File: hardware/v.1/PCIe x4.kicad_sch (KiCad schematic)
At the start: 18 parts, among them J2 Bus_PCI_Express_x4

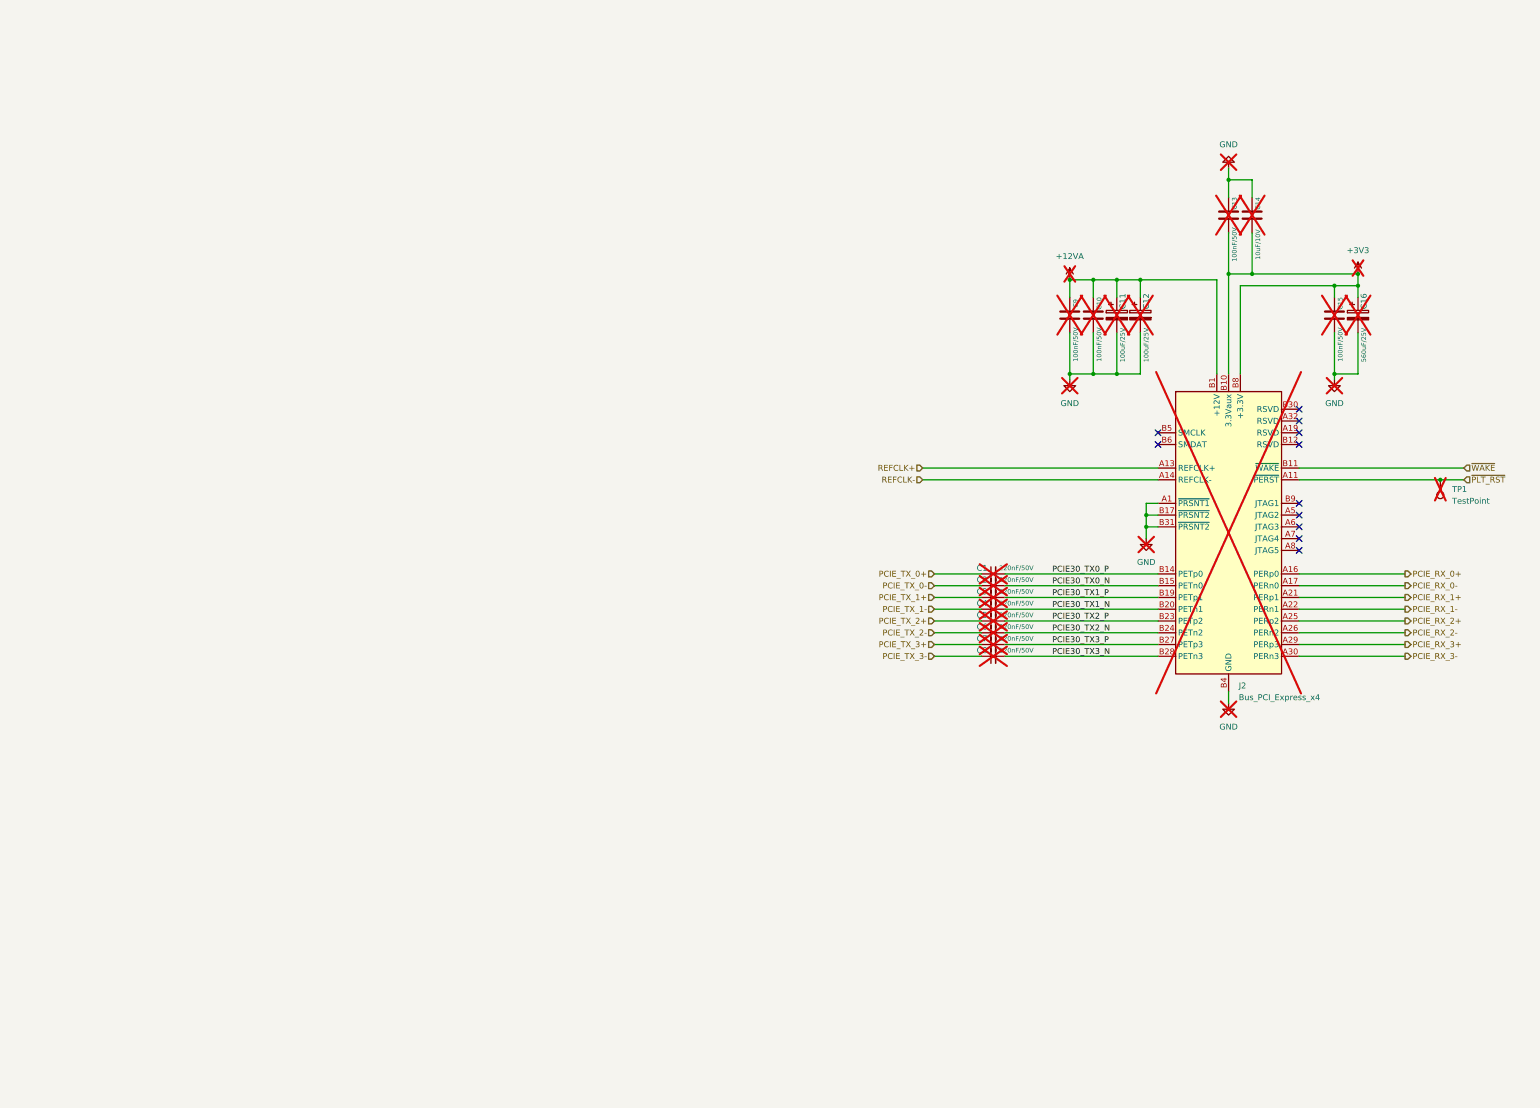
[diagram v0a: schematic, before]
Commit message: pretty much finish the board, did bios chip, gpio, 4x sata
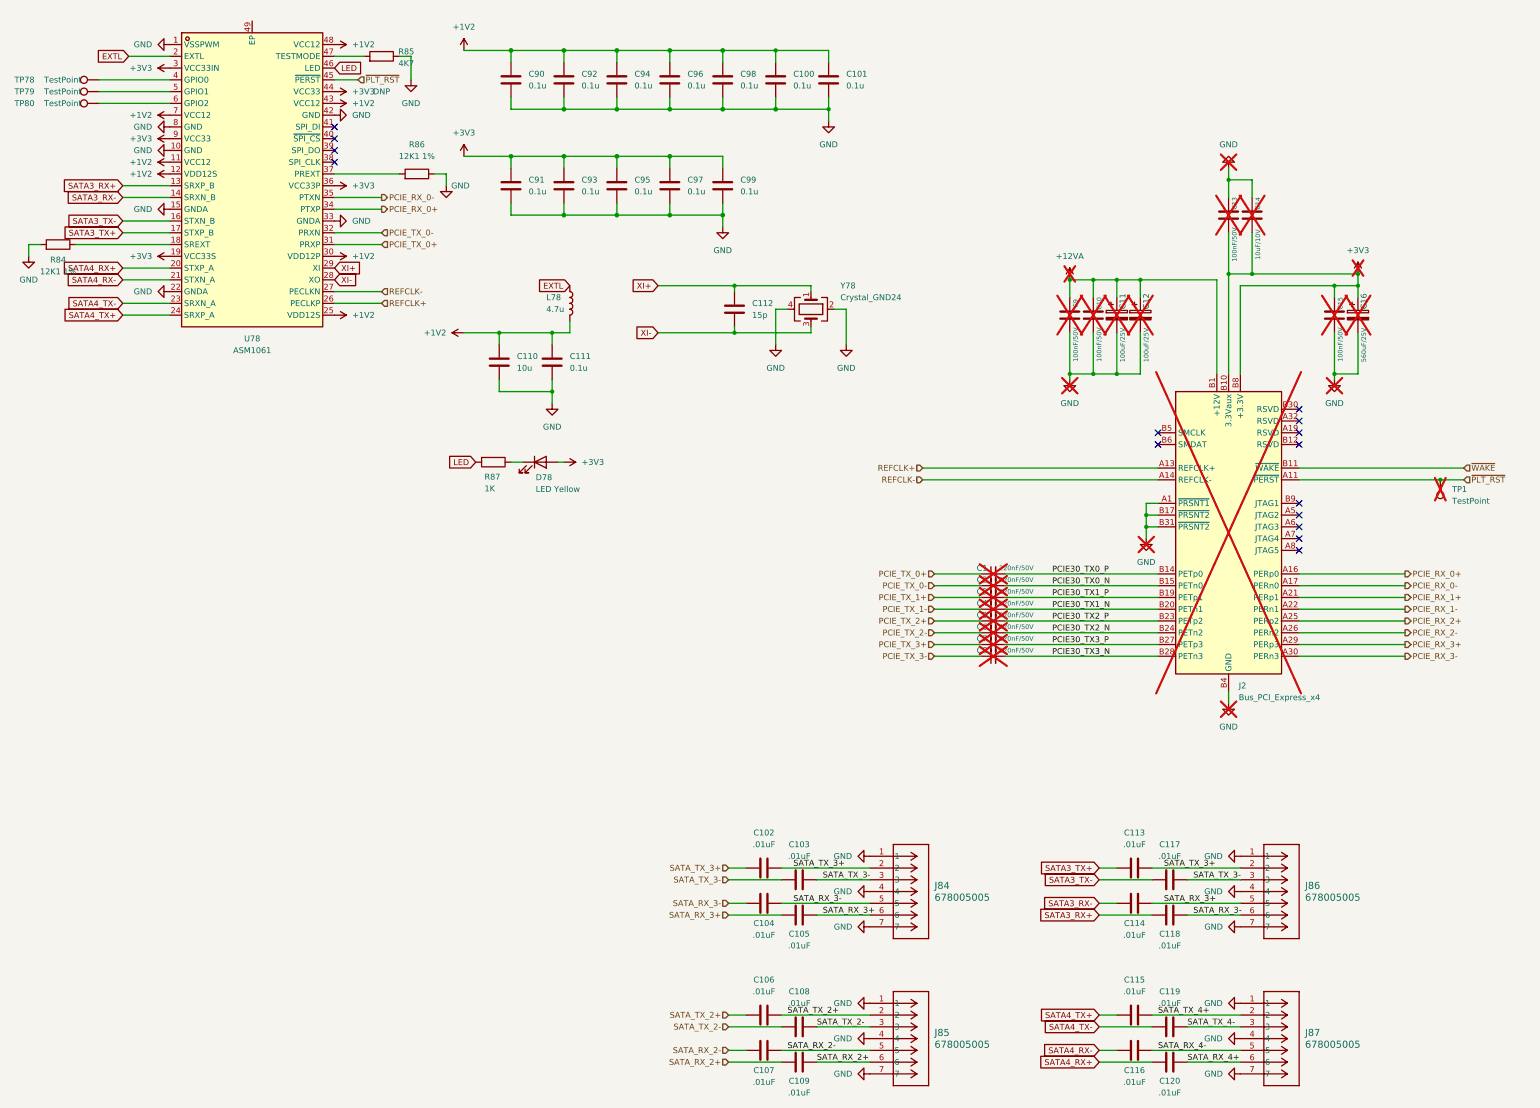
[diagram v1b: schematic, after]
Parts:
- added C100, C101, C111, C90, C91, C92, C93, C94, C95, C96, C97, C98, C99: 0.1u, Capacitor_SMD:C_0402_1005Metric, symbol Device:C
- added C102, C103, C104, C105, C106, C107, C108, C109, C113, C114, C115, C116, C117, C118, C119, C120: .01uF, Capacitor_SMD:C_0402_1005Metric, symbol Device:C
- added C110: 10u, Capacitor_SMD:C_0805_2012Metric, symbol Device:C
- added C112: 15p, Capacitor_SMD:C_0402_1005Metric, symbol Device:C
- added D78: LED Yellow, LED_SMD:LED_0603_1608Metric, symbol Device:LED
- added J84, J85, J86, J87: 678005005, SATA 7PIN:CONN_67800-5005_MOL, symbol 2025-07-27_04-45-58:678005005
- added L78: 4.7u, Inductor_SMD:L_1008_2520Metric, symbol Device:L
- added R84, R86: 12K1 1%, Resistor_SMD:R_0402_1005Metric, symbol Device:R
- added R85: 4K7, Resistor_SMD:R_0402_1005Metric, symbol Device:R
- added R87: 1K, Resistor_SMD:R_0402_1005Metric, symbol Device:R
- added TP78, TP79, TP80: TestPoint, A_HDJ_Library:TestPoint_Pad_D1.5mm, symbol Connector:TestPoint
- added U78: ASM1061, ASM1166:QFN-48_L7.0-W7.0-P0.50-BL-EP4.1, symbol ASM1166:ASM1061
- added Y78: Crystal_GND24, Crystal:Crystal_SMD_3225-4Pin_3.2x2.5mm, symbol Device:Crystal_GND24
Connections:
- net +3V3: now also C91.1, C93.1, C95.1, C97.1, C99.1, D78.2 (A), U78.19 (VCC33S), U78.3 (VCC33IN), U78.36 (VCC33P), U78.44 (VCC33), U78.9 (VCC33)
- net GND: now also C100.2, C101.2, C110.2, C111.2, C90.2, C91.2, C92.2, C93.2, C94.2, C95.2, C96.2, C97.2, C98.2, C99.2, J84.1, J84.4, J84.7, J85.1, J85.4, J85.7, J86.1, J86.4, J86.7, J87.1, J87.4, J87.7, R84.2, R85.1, R86.1, U78.1 (VSSPWM), U78.10 (GND), U78.15 (GNDA), U78.22 (GNDA), U78.33 (GNDA), U78.42 (GND), U78.8 (GND), Y78.2, Y78.4
- net PCIE_RX_0+: now also U78.34 (PTXP)
- net PCIE_RX_0-: now also U78.35 (PTXN)
- net PCIE_TX_0+: now also U78.31 (PRXP)
- net PCIE_TX_0-: now also U78.32 (PRXN)
- net REFCLK+: now also U78.26 (PECLKP)
- net REFCLK-: now also U78.27 (PECLKN)
- net ~{PLT_RST}: now also U78.45 (~{PERST})
- new net: R84.1, U78.18 (SREXT)
- new net: R85.2, U78.47 (TESTMODE)
- new net: TP78.1, U78.4 (GPIO0)
- new net: TP80.1, U78.6 (GPIO2)
- new net: R86.2, U78.37 (PREXT)
- new net: TP79.1, U78.5 (GPIO1)
- new net: D78.1 (K), R87.1
- new net +1V2: C100.1, C101.1, C110.1, C111.1, C90.1, C92.1, C94.1, C96.1, C98.1, L78.2, U78.11 (VCC12), U78.12 (VDD12S), U78.25 (VDD12S), U78.30 (VDD12P), U78.43 (VCC12), U78.48 (VCC12), U78.7 (VCC12)
- new net EXTL: L78.1, U78.2 (EXTL)
- new net LED: R87.2, U78.46 (LED)
- new net SATA3_RX+: C118.1, U78.13 (SRXP_B)
- new net SATA3_RX-: C114.1, U78.14 (SRXN_B)
- new net SATA3_TX+: C113.1, U78.17 (STXP_B)
- new net SATA3_TX-: C117.1, U78.16 (STXN_B)
- new net SATA4_RX+: C120.1, U78.20 (STXP_A)
- new net SATA4_RX-: C116.1, U78.21 (STXN_A)
- new net SATA4_TX+: C115.1, U78.24 (SRXP_A)
- new net SATA4_TX-: C119.1, U78.23 (SRXN_A)
- new net SATA_RX_2+: C109.1, C109.2, J85.6
- new net SATA_RX_2-: C107.1, C107.2, J85.5
- new net SATA_RX_3+: C105.1, C105.2, C114.2, J84.6, J86.5
- new net SATA_RX_3-: C104.1, C104.2, C118.2, J84.5, J86.6
- new net SATA_RX_4+: C120.2, J87.6
- new net SATA_RX_4-: C116.2, J87.5
- new net SATA_TX_2+: C106.1, C106.2, J85.2
- new net SATA_TX_2-: C108.1, C108.2, J85.3
- new net SATA_TX_3+: C102.1, C102.2, C113.2, J84.2, J86.2
- new net SATA_TX_3-: C103.1, C103.2, C117.2, J84.3, J86.3
- new net SATA_TX_4+: C115.2, J87.2
- new net SATA_TX_4-: C119.2, J87.3
- new net XI+: C112.1, U78.29 (XI), Y78.1
- new net XI-: C112.2, U78.28 (XO), Y78.3
- no-connect marks 11 -> 15

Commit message: design review finished: 0.4/0.2 vias changed to 0.4/0.3, VDC polygon and associated reroute, SATA connector, more ground vias, UART testpoints added, fixed unconnects; DRC at minimum. The BIOS sheet is faulty here (causing all remaining DRC errors)
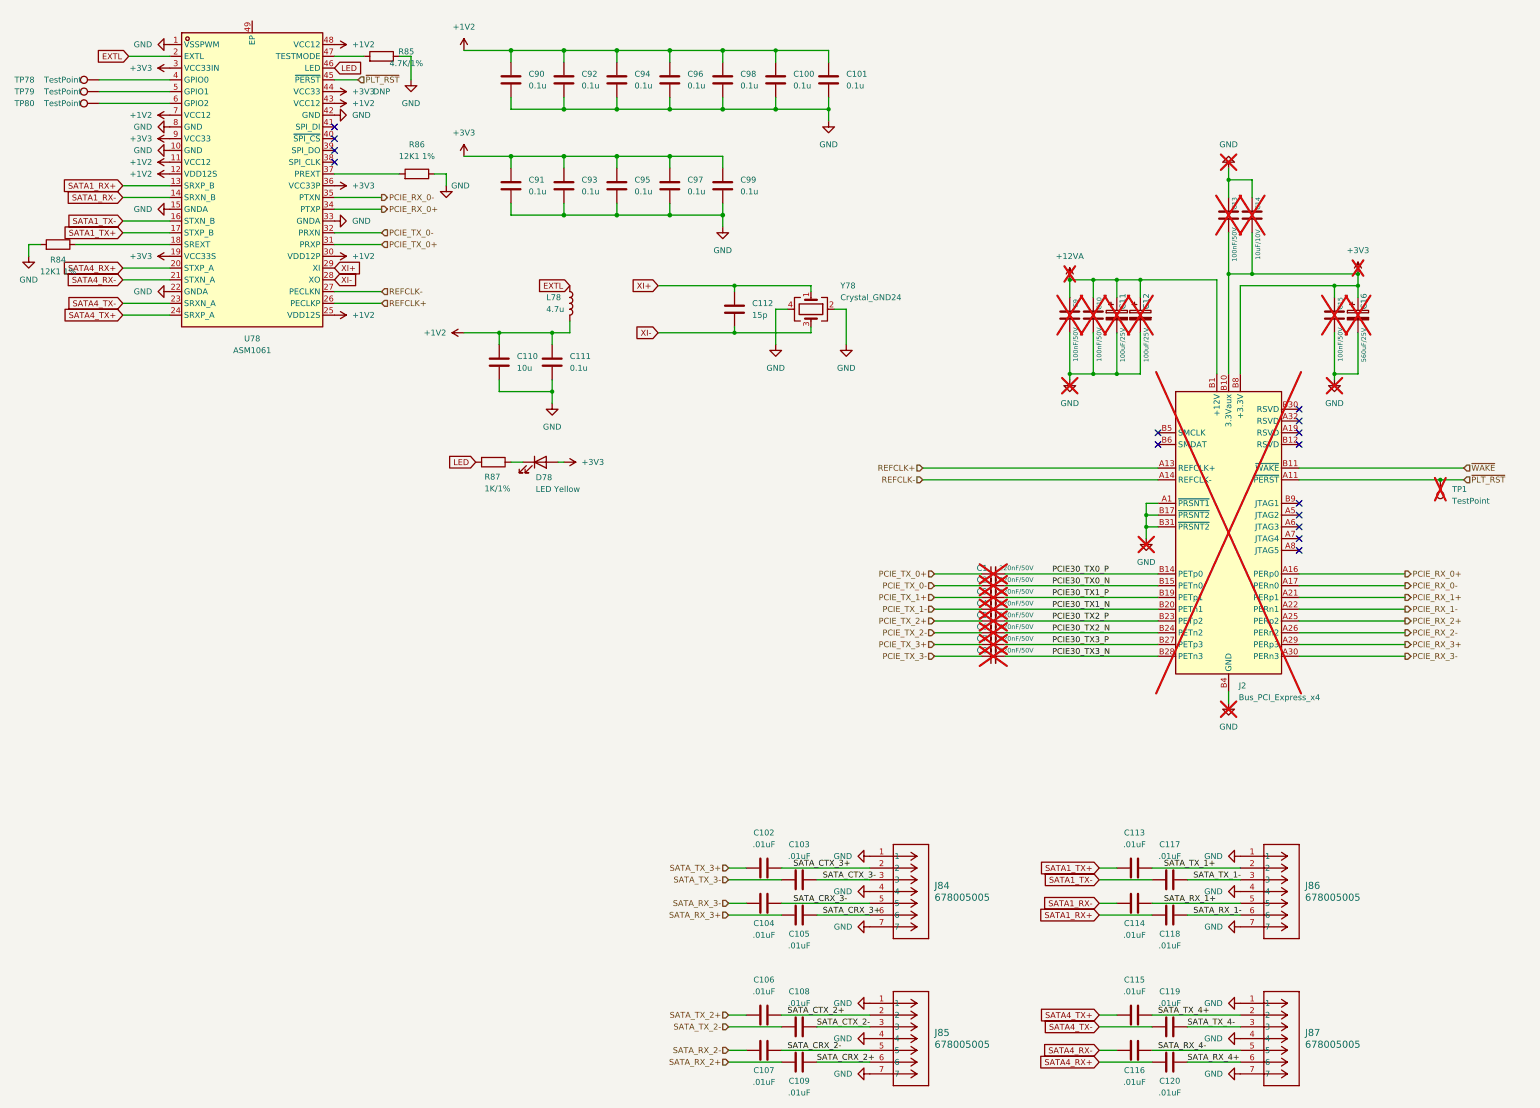
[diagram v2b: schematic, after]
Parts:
- J84, J85, J86, J87: footprint SATA 7PIN:CONN_67800-5005_MOL -> A_HDJ_Library:CONN_67800-5005_MOL
- R85: value 4K7 -> 4.7K/1%
- R87: value 1K -> 1K/1%
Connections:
- net SATA_RX_2+: no longer C109.1, J85.6
- net SATA_RX_2-: no longer C107.1, J85.5
- net SATA_RX_3+: no longer C105.2, C114.2, J84.6, J86.5
- net SATA_RX_3-: no longer C104.2, C118.2, J84.5, J86.6
- net SATA_TX_2+: no longer C106.1, J85.2
- net SATA_TX_2-: no longer C108.1, J85.3
- net SATA_TX_3+: no longer C102.2, C113.2, J84.2, J86.2
- net SATA_TX_3-: no longer C103.2, C117.2, J84.3, J86.3
- net SATA3_RX+ renamed SATA1_RX+
- net SATA3_RX- renamed SATA1_RX-
- net SATA3_TX+ renamed SATA1_TX+
- net SATA3_TX- renamed SATA1_TX-
- new net SATA_CRX_2+: C109.1, J85.6
- new net SATA_CRX_2-: C107.1, J85.5
- new net SATA_CRX_3+: C105.2, J84.6
- new net SATA_CRX_3-: C104.2, J84.5
- new net SATA_CTX_2+: C106.1, J85.2
- new net SATA_CTX_2-: C108.1, J85.3
- new net SATA_CTX_3+: C102.2, J84.2
- new net SATA_CTX_3-: C103.2, J84.3
- new net SATA_RX_1+: C114.2, J86.5
- new net SATA_RX_1-: C118.2, J86.6
- new net SATA_TX_1+: C113.2, J86.2
- new net SATA_TX_1-: C117.2, J86.3
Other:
- moved on the sheet: C106, C107, C108, C109
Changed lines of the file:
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@@
 		)
 	)
-	(label "SATA_TX_3+"
+	(label "SATA_TX_1+"
 		(at 303.53 294.64 0)
 		(effects
@@
 		)
 	)
-	(label "SATA_RX_3+"
+	(label "SATA_CRX_3+"
 		(at 229.87 304.8 0)
 		(effects
@@
 		)
 	)
-	(label "SATA_RX_2-"
+	(label "SATA_CRX_2-"
 		(at 222.25 334.01 0)
 		(effects
@@
 		)
 	)
-	(label "SATA_TX_3-"
+	(label "SATA_TX_1-"
 		(at 309.88 297.18 0)
 		(effects
@@
 		)
 	)
-	(label "SATA_RX_3-"
+	(label "SATA_CRX_3-"
 		(at 223.52 302.26 0)
 		(effects
@@
 		)
 	)
-	(label "SATA_RX_3-"
+	(label "SATA_RX_1-"
 		(at 309.88 304.8 0)
 		(effects
@@
 		)
 	)
-	(label "SATA_RX_3+"
+	(label "SATA_RX_1+"
 		(at 303.53 302.26 0)
 		(effects
@@
 		)
 	)
-	(label "SATA_TX_3-"
+	(label "SATA_CTX_3-"
 		(at 229.87 297.18 0)
 		(effects
@@
 		)
 	)
-	(label "SATA_TX_2+"
+	(label "SATA_CTX_2+"
 		(at 222.25 326.39 0)
 		(effects
@@
 		)
 	)
-	(label "SATA_TX_2-"
+	(label "SATA_CTX_2-"
 		(at 228.6 328.93 0)
 		(effects
@@
 		)
 	)
-	(label "SATA_RX_2+"
+	(label "SATA_CRX_2+"
 		(at 228.6 336.55 0)
 		(effects
@@
 		)
 	)
-	(label "SATA_TX_3+"
+	(label "SATA_CTX_3+"
 		(at 223.52 294.64 0)
 		(effects
@@
 		)
 	)
-	(global_label "SATA3_RX+"
+	(global_label "SATA1_RX+"
 		(shape input)
 		(at 289.56 304.8 180)
@@
 		)
 	)
-	(global_label "SATA3_RX-"
+	(global_label "SATA1_RX-"
 		(shape input)
 		(at 289.56 302.26 180)
@@
 		)
 	)
-	(global_label "SATA3_RX-"
+	(global_label "SATA1_RX-"
 		(shape input)
 		(at 78.74 149.86 180)
@@
 		)
 	)
-	(global_label "SATA3_TX+"
+	(global_label "SATA1_TX+"
 		(shape input)
 		(at 78.74 157.48 180)
@@
 		)
 	)
-	(global_label "SATA3_TX-"
+	(global_label "SATA1_TX-"
 		(shape input)
 		(at 289.56 297.18 180)
@@
 		)
 	)
-	(global_label "SATA3_TX+"
+	(global_label "SATA1_TX+"
 		(shape input)
 		(at 289.56 294.64 180)
@@
 		)
 	)
-	(global_label "SATA3_RX+"
+	(global_label "SATA1_RX+"
 		(shape input)
 		(at 78.74 147.32 180)
@@
 		)
 	)
-	(global_label "SATA3_TX-"
+	(global_label "SATA1_TX-"
 		(shape input)
 		(at 78.74 154.94 180)
@@
 			)
 		)
-		(property "Value" "4K7"
+		(property "Value" "4.7K/1%"
 			(at 139.954 120.904 90)
 			(effects
@@
 		(on_board yes)
 		(dnp no)
-		(fields_autoplaced yes)
 		(property "Reference" "C102"
 			(at 217.17 287.02 90)
@@
 		(on_board yes)
 		(dnp no)
-		(fields_autoplaced yes)
 		(property "Reference" "C103"
 			(at 224.79 289.56 90)
@@
 			)
 		)
-		(property "Footprint" "SATA 7PIN:CONN_67800-5005_MOL"
+		(property "Footprint" "A_HDJ_Library:CONN_67800-5005_MOL"
 			(at 240.03 323.85 0)
 			(effects
@@
 			)
 		)
-		(property "Footprint" "SATA 7PIN:CONN_67800-5005_MOL"
+		(property "Footprint" "A_HDJ_Library:CONN_67800-5005_MOL"
 			(at 320.04 292.1 0)
 			(effects
@@
 			)
 		)
-		(property "Footprint" "SATA 7PIN:CONN_67800-5005_MOL"
+		(property "Footprint" "A_HDJ_Library:CONN_67800-5005_MOL"
 			(at 240.03 292.1 0)
 			(effects
@@
 	(symbol
 		(lib_id "Device:C")
-		(at 224.79 336.55 90)
+		(at 224.79 336.55 270)
+		(mirror x)
 		(unit 1)
 		(exclude_from_sim no)
@@
 		)
 		(property "Footprint" "Capacitor_SMD:C_0402_1005Metric"
-			(at 228.6 335.5848 0)
+			(at 220.98 335.5848 0)
 			(effects
 				(font
@@
 	(symbol
 		(lib_id "Device:C")
-		(at 217.17 326.39 90)
+		(at 217.17 326.39 270)
+		(mirror x)
 		(unit 1)
 		(exclude_from_sim no)
@@
 		(on_board yes)
 		(dnp no)
-		(fields_autoplaced yes)
 		(property "Reference" "C106"
 			(at 217.17 318.77 90)
@@
 		)
 		(property "Footprint" "Capacitor_SMD:C_0402_1005Metric"
-			(at 220.98 325.4248 0)
+			(at 213.36 325.4248 0)
 			(effects
 				(font
@@
 			)
 		)
-		(property "Value" "1K"
+		(property "Value" "1K/1%"
 			(at 156.845 212.7249 90)
 			(effects
@@
 			)
 		)
-		(property "Footprint" "SATA 7PIN:CONN_67800-5005_MOL"
+		(property "Footprint" "A_HDJ_Library:CONN_67800-5005_MOL"
 			(at 320.04 323.85 0)
 			(effects
@@
 	(symbol
 		(lib_id "Device:C")
-		(at 224.79 328.93 90)
+		(at 224.79 328.93 270)
+		(mirror x)
 		(unit 1)
 		(exclude_from_sim no)
@@
 		(on_board yes)
 		(dnp no)
-		(fields_autoplaced yes)
 		(property "Reference" "C108"
 			(at 224.79 321.31 90)
@@
 		)
 		(property "Footprint" "Capacitor_SMD:C_0402_1005Metric"
-			(at 228.6 327.9648 0)
+			(at 220.98 327.9648 0)
 			(effects
 				(font
@@
 	(symbol
 		(lib_id "Device:C")
-		(at 217.17 334.01 90)
+		(at 217.17 334.01 270)
+		(mirror x)
 		(unit 1)
 		(exclude_from_sim no)
@@
 		)
 		(property "Footprint" "Capacitor_SMD:C_0402_1005Metric"
-			(at 220.98 333.0448 0)
+			(at 213.36 333.0448 0)
 			(effects
 				(font

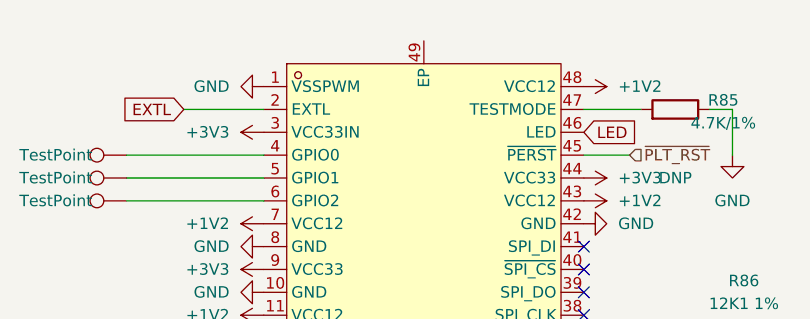
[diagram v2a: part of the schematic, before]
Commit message: add cad models for components, silkscreen labeling, fix asm1061 ground pour
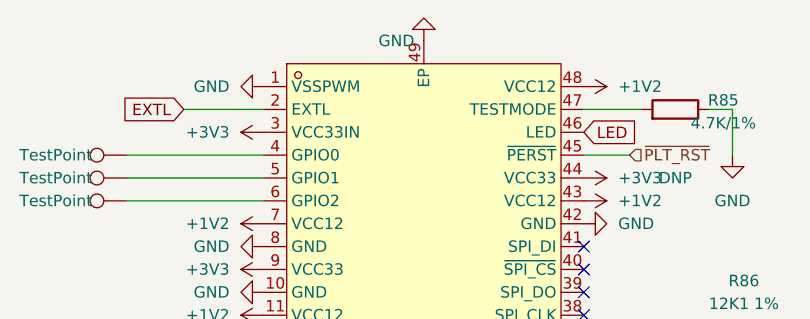
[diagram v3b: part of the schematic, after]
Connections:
- net GND: now also U78.49 (EP)
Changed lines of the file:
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@@
+	)
+	(symbol
+		(lib_id "power:GND")
+		(at 106.68 111.76 0)
+		(mirror x)
+		(unit 1)
+		(exclude_from_sim no)
+		(in_bom yes)
+		(on_board yes)
+		(dnp no)
+		(property "Reference" "#PWR0121"
+			(at 106.68 105.41 0)
+			(effects
+				(font
+					(size 1.27 1.27)
+				)
+				(hide yes)
+			)
+		)
+		(property "Value" "GND"
+			(at 103.632 111.76 0)
+			(effects
+				(font
+					(size 1.27 1.27)
+				)
+			)
+		)
+		(property "Footprint" ""
+			(at 106.68 111.76 0)
+			(effects
+				(font
+					(size 1.27 1.27)
+				)
+				(hide yes)
+			)
+		)
+		(property "Datasheet" ""
+			(at 106.68 111.76 0)
+			(effects
+				(font
+					(size 1.27 1.27)
+				)
+				(hide yes)
+			)
+		)
+		(property "Description" ""
+			(at 106.68 111.76 0)
+			(effects
+				(font
+					(size 1.27 1.27)
+				)
+			)
+		)
+		(pin "1"
+		)
+		(instances
+			(project "[DFR1142]Lite Carrier for LattePanda Mu"
+				(path "/2a6d114a-7fd7-4207-b5f7-4ea9c34f36aa/0716e4e5-1aca-46b3-961a-42a6c1122566"
+					(reference "#PWR0121")
+					(unit 1)
+				)
+			)
+		)
 	)
 	(symbol
